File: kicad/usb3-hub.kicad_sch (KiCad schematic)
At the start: 9 parts, among them J101 DISPLAY, J102 USB3_B_Micro, J103 Barrel_Jack_Switch

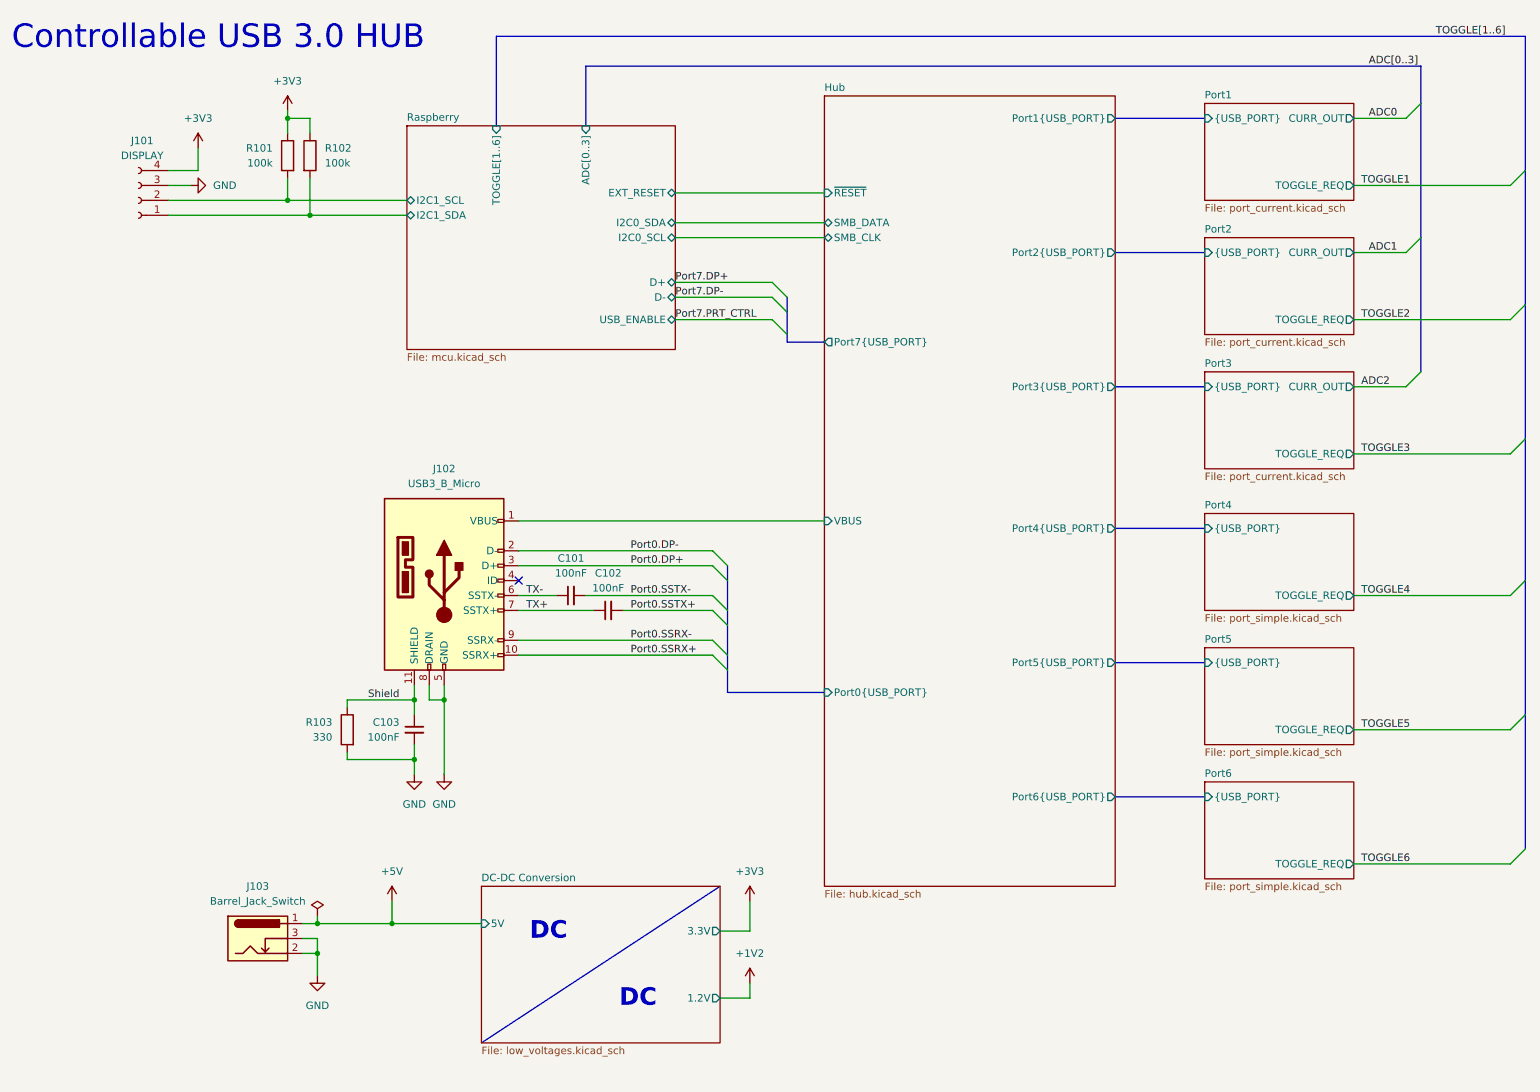
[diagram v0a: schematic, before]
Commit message: First rough placement
Just to get an idea on how it might look like
Added trace widts for Differential pairs
Using 6 layers, because it makes power management easier.
Rather large PCB, but better to big, then to small.
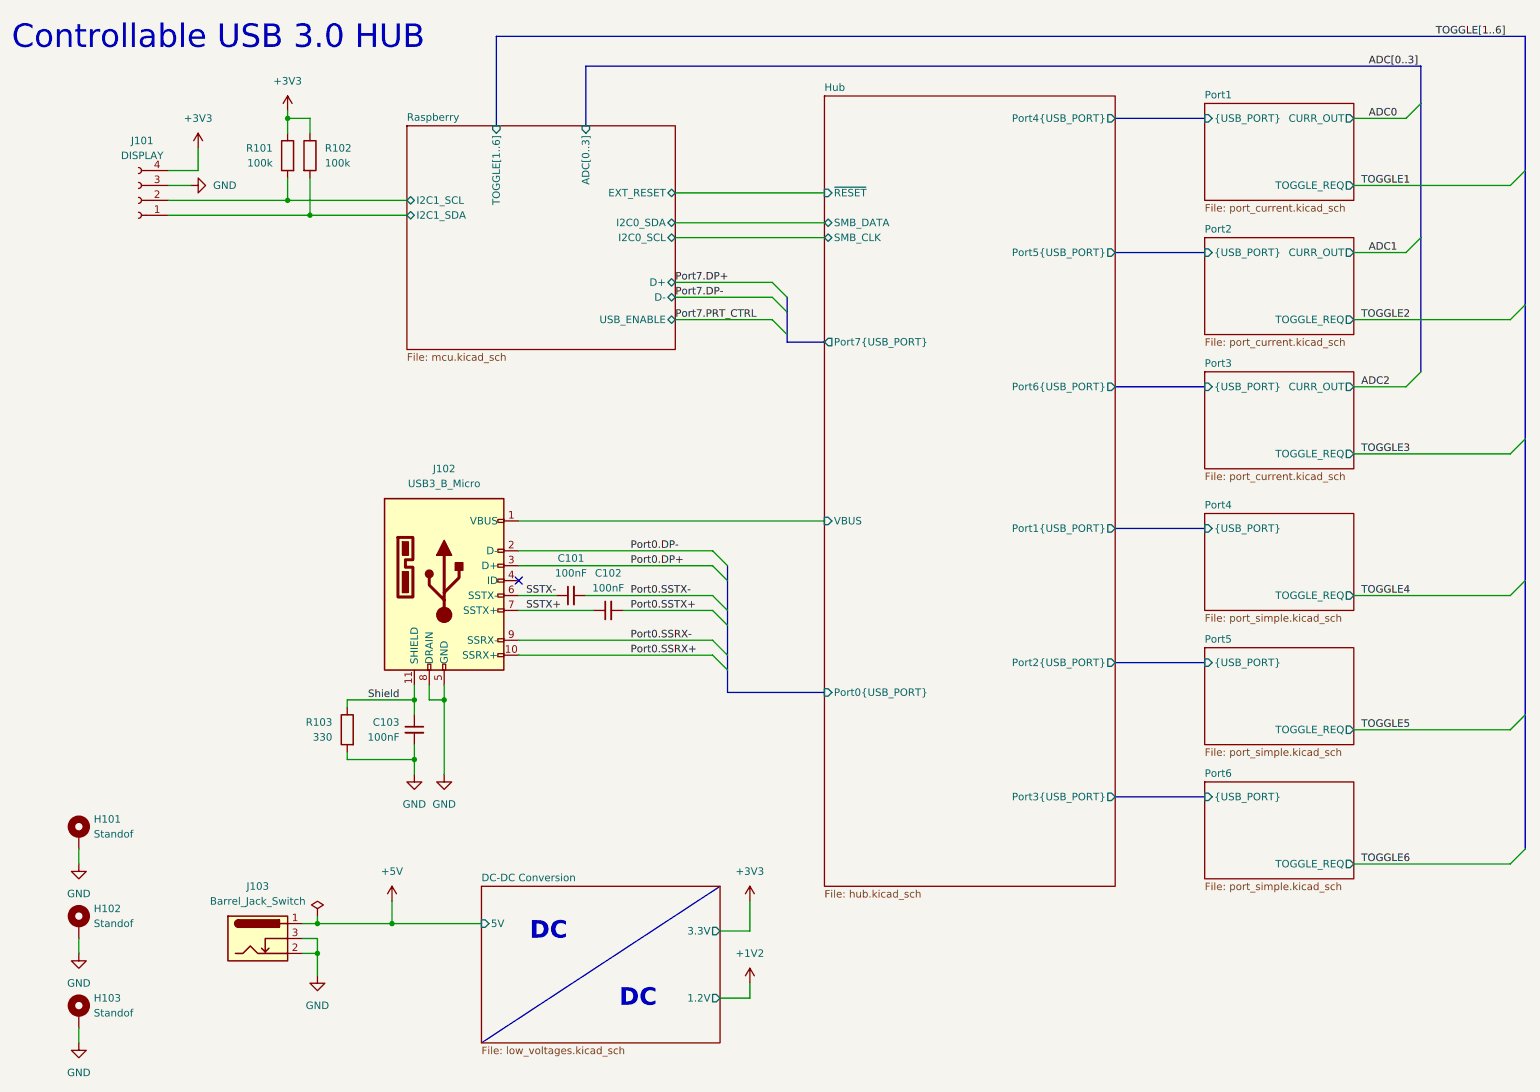
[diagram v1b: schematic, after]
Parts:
- added H101, H102, H103: Standof, MountingHole:MountingHole_3.2mm_M3_DIN965_Pad_TopOnly, symbol Mechanical:MountingHole_Pad
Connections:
- net GND: now also H101.1, H102.1, H103.1
- net TX+ renamed SSTX+
- net TX- renamed SSTX-

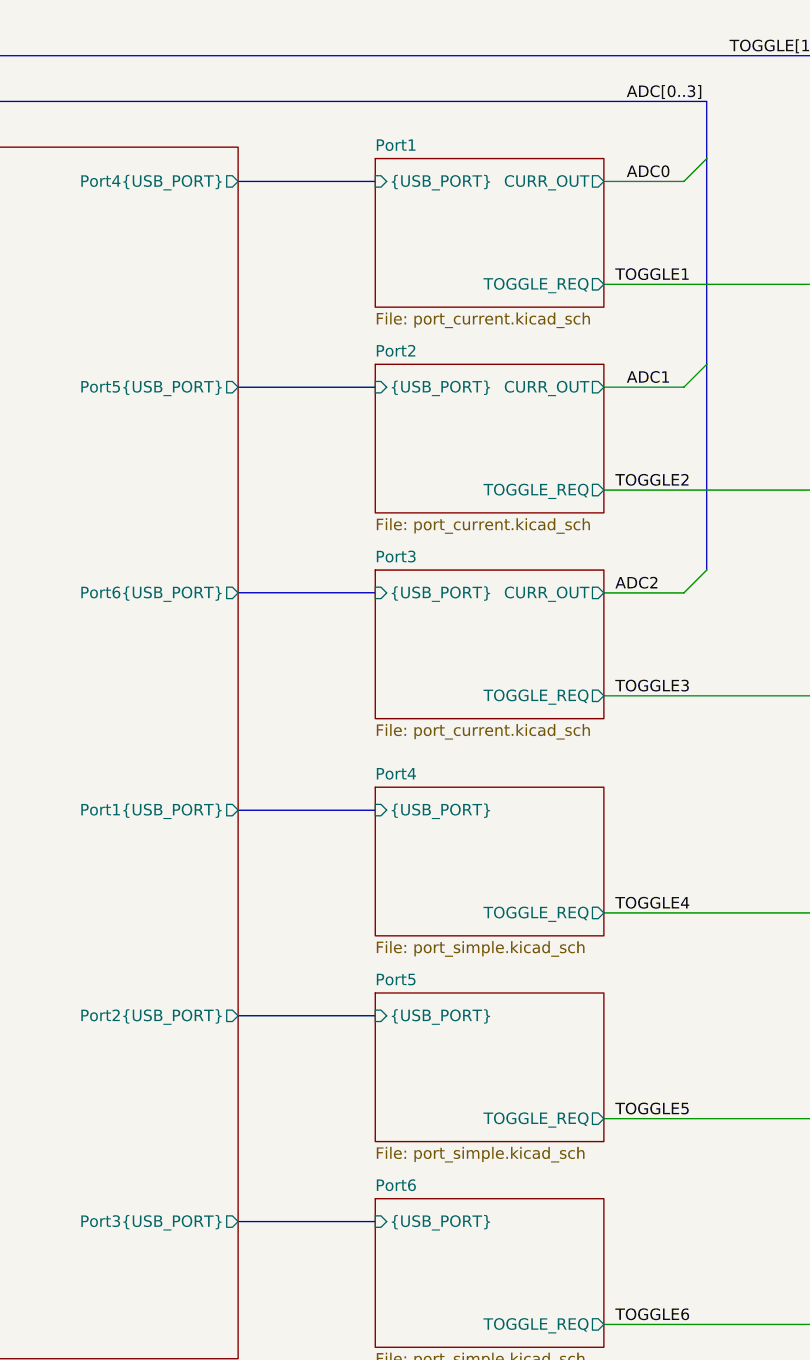
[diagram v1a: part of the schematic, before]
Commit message: Added first fanout for usb5807
Needs a lot more work, but it is a start, that allows me to concentrate
on the routing of USB signals and have the capacitors relatively close
to the hub controller.
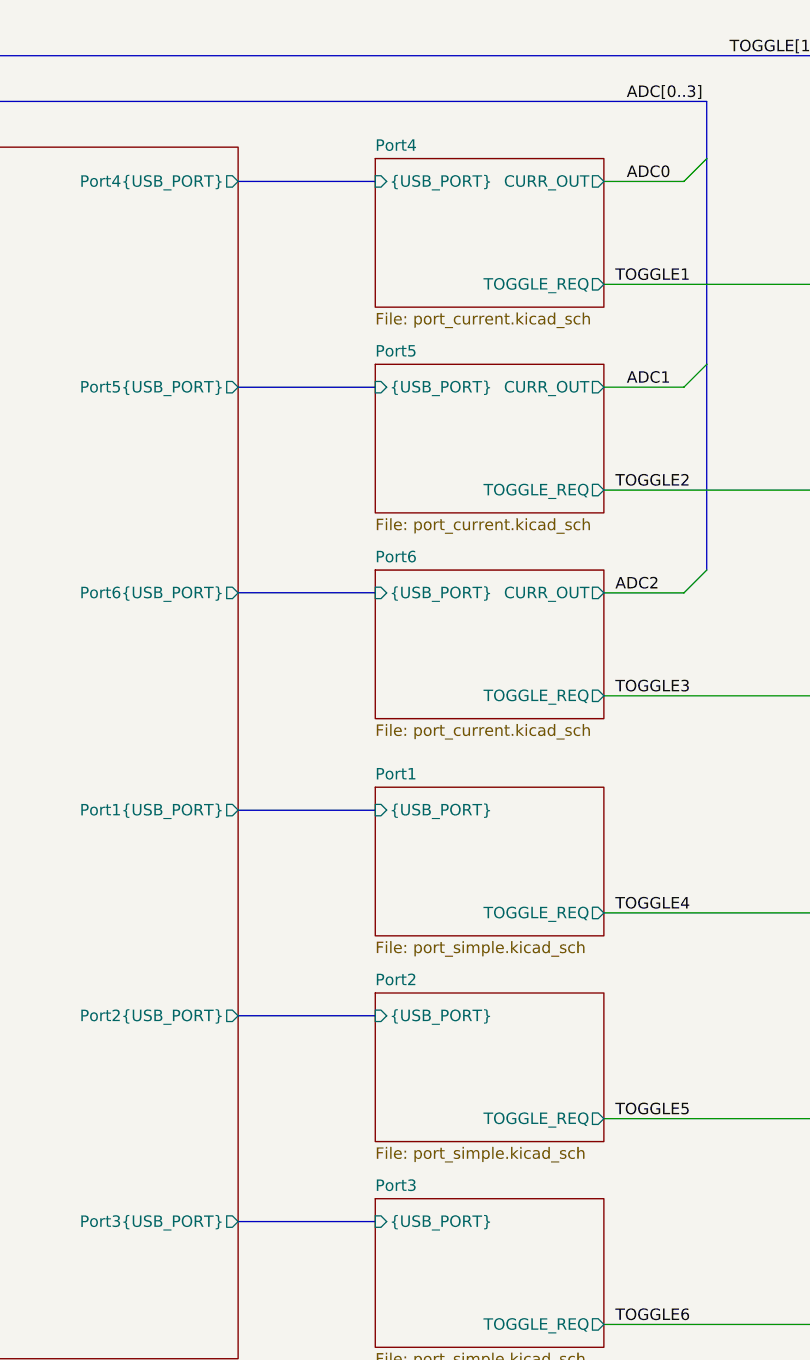
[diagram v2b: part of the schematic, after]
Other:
- sheet Port1: file port_current.kicad_sch -> port_simple.kicad_sch
- sheet Port1 ports: added none; removed CURR_OUT
- sheet Port2: file port_current.kicad_sch -> port_simple.kicad_sch
- sheet Port2 ports: added none; removed CURR_OUT
- sheet Port3: file port_current.kicad_sch -> port_simple.kicad_sch
- sheet Port3 ports: added none; removed CURR_OUT
- sheet Port4: file port_simple.kicad_sch -> port_current.kicad_sch
- sheet Port4 ports: added CURR_OUT; removed none
- sheet Port5: file port_simple.kicad_sch -> port_current.kicad_sch
- sheet Port5 ports: added CURR_OUT; removed none
- sheet Port6: file port_simple.kicad_sch -> port_current.kicad_sch
- sheet Port6 ports: added CURR_OUT; removed none
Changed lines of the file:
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@@
 			(color 195 255 238 1.0000)
 		)
-		(property "Sheetname" "Port5"
+		(property "Sheetname" "Port2"
 			(at 217.17 119.9384 0)
 			(effects
@@
 			(color 195 255 238 1.0000)
 		)
-		(property "Sheetname" "Port4"
+		(property "Sheetname" "Port1"
 			(at 217.17 97.0784 0)
 			(effects
@@
 			(color 213 255 203 1.0000)
 		)
-		(property "Sheetname" "Port3"
+		(property "Sheetname" "Port6"
 			(at 217.17 72.9484 0)
 			(effects
@@
 			(color 213 255 203 1.0000)
 		)
-		(property "Sheetname" "Port1"
+		(property "Sheetname" "Port4"
 			(at 217.17 27.2284 0)
 			(effects
@@
 			(color 195 255 238 1.0000)
 		)
-		(property "Sheetname" "Port6"
+		(property "Sheetname" "Port3"
 			(at 217.17 142.7984 0)
 			(effects
@@
 			(color 213 255 203 1.0000)
 		)
-		(property "Sheetname" "Port2"
+		(property "Sheetname" "Port5"
 			(at 217.17 50.0884 0)
 			(effects

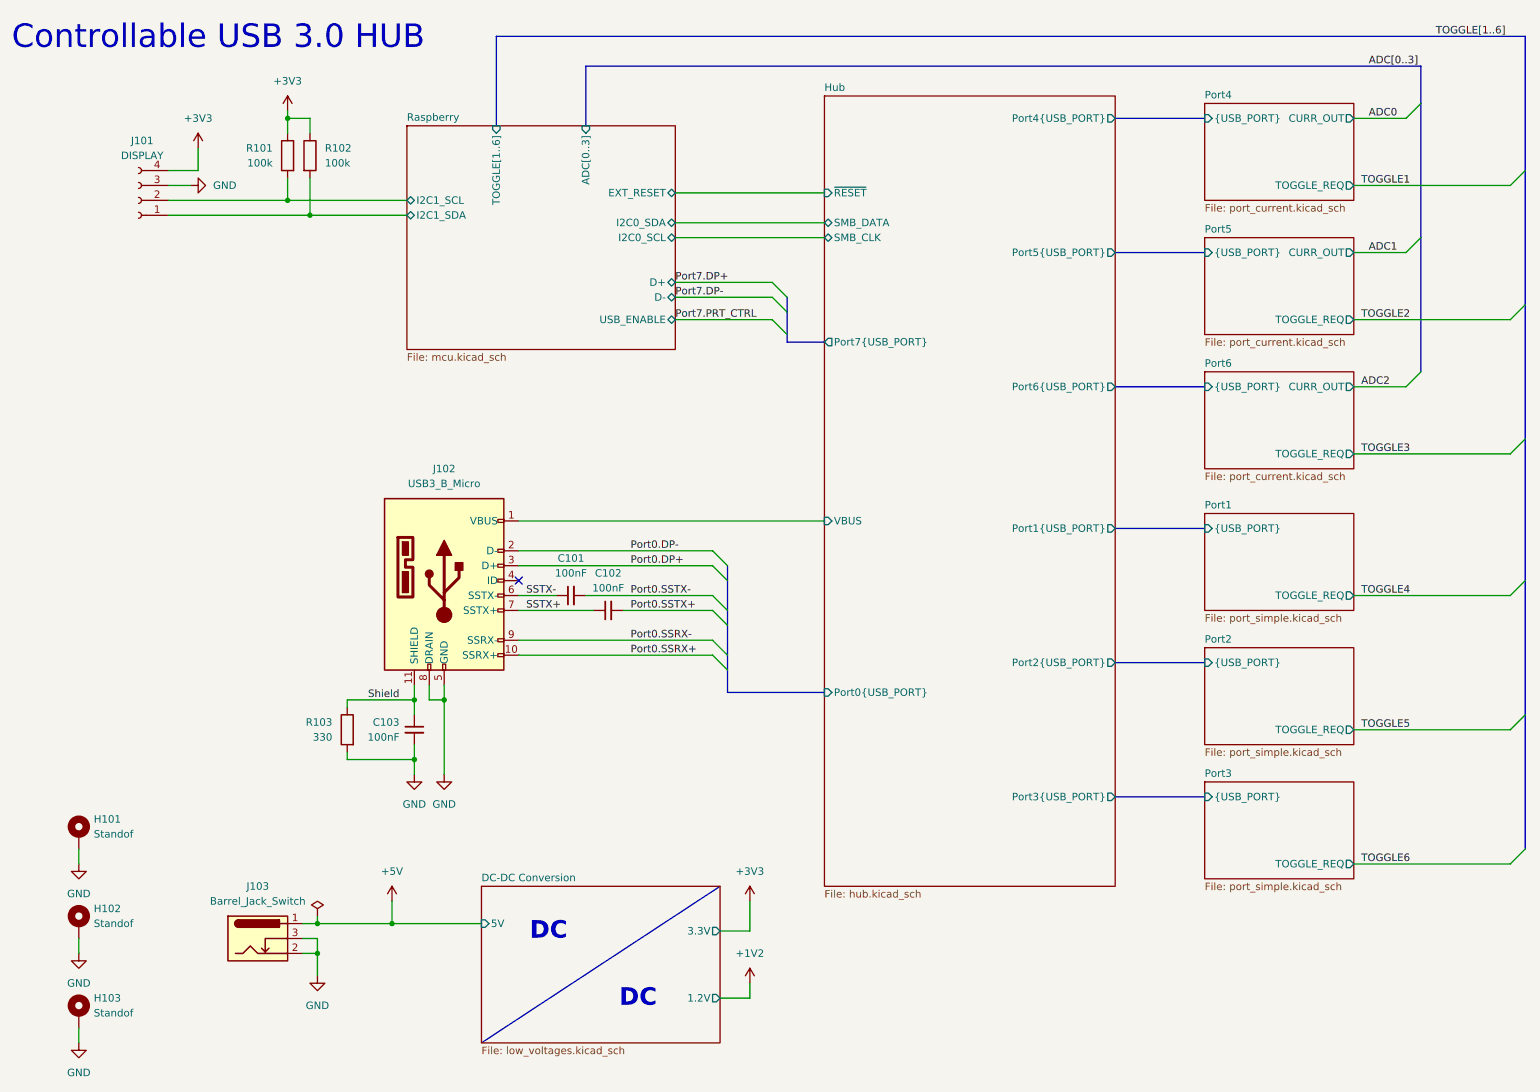
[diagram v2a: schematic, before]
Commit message: Some more routing
Not done, but done some more. Nothing is final, just to get a
better feeling of what could be done.
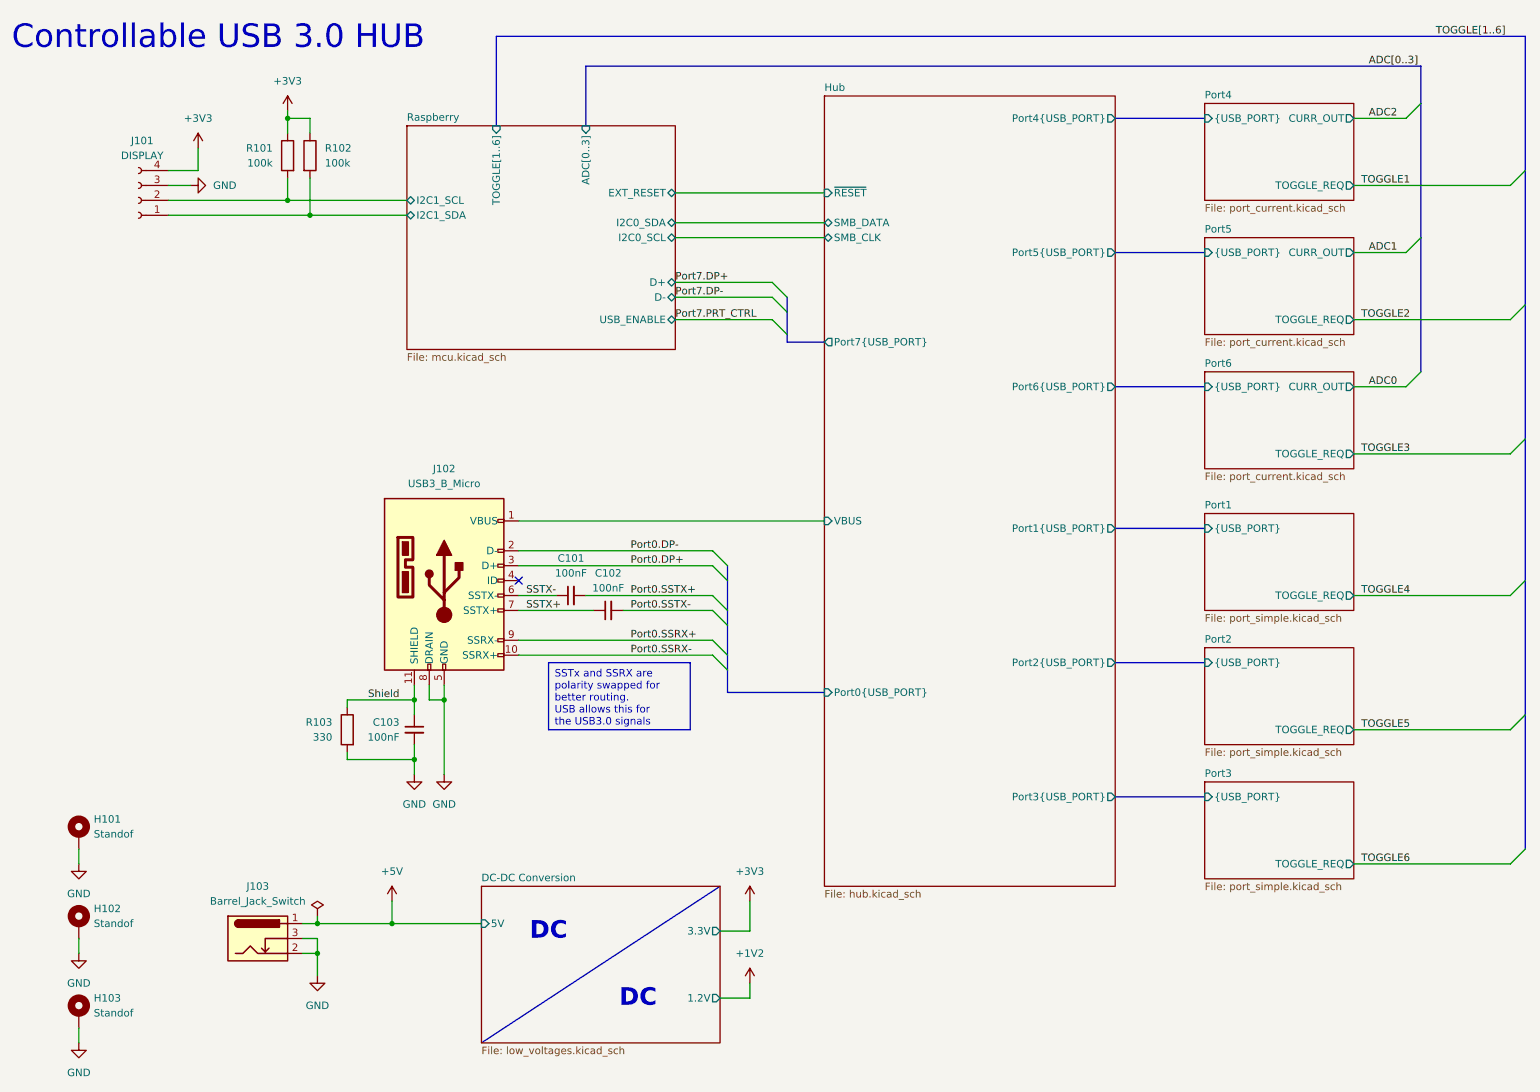
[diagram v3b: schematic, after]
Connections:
- net Port0.SSRX+: now also J102.9 (SSRX-); no longer J102.10 (SSRX+)
- net Port0.SSRX-: now also J102.10 (SSRX+); no longer J102.9 (SSRX-)
- net Port0.SSTX+: now also C101.2; no longer C102.2
- net Port0.SSTX-: now also C102.2; no longer C101.2
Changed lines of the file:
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@@
+		)
+	)
+	(text_box "SSTx and SSRX are polarity swapped for better routing.\nUSB allows this for the USB3.0 signals"
+		(exclude_from_sim no)
+		(at 105.41 123.19 0)
+		(size 24.13 11.43)
+		(stroke
+			(width 0)
+			(type default)
+		)
+		(fill
+			(type none)
+		)
+		(effects
+			(font
+				(size 1.27 1.27)
+			)
+			(justify left top)
 		)
 	)
@@
 	)
 	(label "Port0.SSTX+"
-		(at 119.38 114.3 0)
+		(at 119.38 111.76 0)
 		(fields_autoplaced yes)
 		(effects
@@
 	)
 	(label "ADC0"
-		(at 245.11 30.48 0)
+		(at 245.11 76.2 0)
 		(fields_autoplaced yes)
 		(effects
@@
 	)
 	(label "Port0.SSTX-"
-		(at 119.38 111.76 0)
+		(at 119.38 114.3 0)
 		(fields_autoplaced yes)
 		(effects
@@
 	)
 	(label "ADC2"
-		(at 243.84 76.2 0)
+		(at 245.11 30.48 0)
 		(fields_autoplaced yes)
 		(effects
@@
 	)
 	(label "Port0.SSRX-"
+		(at 119.38 121.92 0)
+		(fields_autoplaced yes)
+		(effects
+			(font
+				(size 1.27 1.27)
+			)
+			(justify left bottom)
+		)
+	)
+	(label "Port0.SSRX+"
 		(at 119.38 119.38 0)
 		(fields_autoplaced yes)
 		(effects
-			(font
-				(size 1.27 1.27)
-			)
-			(justify left bottom)
-		)
-	)
-	(label "Port0.SSRX+"
-		(at 119.38 121.92 0)
-		(fields_autoplaced yes)
-		(effects
